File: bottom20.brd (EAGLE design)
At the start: 160 x 100 mm, 141 parts

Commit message: - bot.sch (corrections)
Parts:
- removed 5V-SCHALTREGLER1:C3: 100uF, 16V, ±20 %, iceberg20:CAPACITOR-THT-6.3
- removed 5V-SCHALTREGLER1:C4: 1000uF, 25V, ±20 %, iceberg20:CAPACITOR-THT-10
- removed 5V-SCHALTREGLER1:D1: 1N5822, iceberg20:DO-201AD
- removed 5V-SCHALTREGLER1:IC2: LM2576, iceberg20:TO220-5PIN
- removed 5V-SCHALTREGLER1:L1: L-100U, iceberg20:PISR
- removed 5V-SCHALTREGLER1:R1: 100k, iceberg20:R0805
- removed ARDUINO1:R4: 1k, iceberg20:R0805
- added ANSCHLUSS1:J1: 5V-ARD, iceberg20:JUMPER-SJ-3
- added PHOTOTRANSISTOR1:R17, PHOTOTRANSISTOR2:R17: 330, iceberg20:R0805
- added SCHALTREGLER1:X3: SCHALTREGLER, iceberg20:5X1
- ANSCHLUSS1:X1: value FTDI-Adapter -> FTDI
- ANSCHLUSS1:X2: value CON-UP -> WANNENSTECKER-14; device iceberg20:PIN-HEADER-ANGLED-6 -> iceberg20:2X7
- ARDUINO1:R3: value R -> 330
- moved ARDUINO1:C7 1574.2 mm to (-12.4, 20.6)
- moved ARDUINO1:IC1 1574.2 mm to (-22.6, 24.4)
- moved PHOTOTRANSISTOR2:T9 1515.7 mm to (-7.25, 0.00)
- moved PHOTOTRANSISTOR2:T8 1491.3 mm to (0.00, -58.0), turned to 90 degrees
- moved PHOTOTRANSISTOR2:T7 1488.4 mm to (0.00, -51.2), turned to 90 degrees
- moved PHOTOTRANSISTOR2:T6 1485.7 mm to (0.00, -44.0), turned to 90 degrees
- moved PHOTOTRANSISTOR2:T5 1483.4 mm to (0.00, -36.2), turned to 90 degrees
- moved PHOTOTRANSISTOR2:T4 1480.8 mm to (0.00, -29.0), turned to 90 degrees
- moved PHOTOTRANSISTOR2:T3 1478.1 mm to (0.00, -22.2), turned to 90 degrees
- moved PHOTOTRANSISTOR2:T2 1475.7 mm to (0.00, -15.0), turned to 90 degrees
- moved PHOTOTRANSISTOR2:T1 1434.2 mm to (0.00, -7.25), turned to 90 degrees
- moved PHOTOTRANSISTOR2:T10 1430.0 mm to (-15.0, 0.00)
- moved PHOTOTRANSISTOR2:T11 1429.2 mm to (-22.2, 0.00)
- moved PHOTOTRANSISTOR2:T12 1428.8 mm to (-29.0, 0.00)
- moved PHOTOTRANSISTOR2:T13 1428.0 mm to (-36.2, 0.00)
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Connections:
- net ARDUINO1:D10 renamed ARDUINO1:SS
- removed net 5V-SCHALTREGLER1:N$1: 5V-SCHALTREGLER1:IC2.5, 5V-SCHALTREGLER1:R1.1
- removed net 5V-SCHALTREGLER1:N$2: 5V-SCHALTREGLER1:D1.1, 5V-SCHALTREGLER1:IC2.2, 5V-SCHALTREGLER1:L1.1
- removed net ANSCHLUSS1:N$1: ANSCHLUSS1:X2.P$5
- removed net ARD-IN: ANSCHLUSS1:X2.P$1, ARDUINO1:IC1.10
- removed net ARD-RST: ANSCHLUSS1:X1.P$6, ARDUINO1:C1.1
- removed net ARDUINO1:N$1: ARDUINO1:C1.2, ARDUINO1:IC1.29, ARDUINO1:R3.1, ARDUINO1:S1.A1, ARDUINO1:S1.A2
- removed net BIT0: PHOTOTRANSISTOR2:IC1.11
- removed net BIT1: PHOTOTRANSISTOR2:IC1.10
- removed net BIT2: PHOTOTRANSISTOR2:IC1.14
- removed net BIT3: PHOTOTRANSISTOR2:IC1.13
- removed net BITA0: ARDUINO1:IC1.23
- removed net BITA1: ARDUINO1:IC1.24
- removed net BITA2: ARDUINO1:IC1.25
- removed net BITA3: ARDUINO1:IC1.26
- removed net BITB0: ARDUINO1:IC1.2
- removed net BITB1: ARDUINO1:IC1.9
- removed net BITB2: ARDUINO1:IC1.12
- removed net BITB3: ARDUINO1:IC1.13
- removed net PHOTOTRANSISTOR1:BIT0: PHOTOTRANSISTOR1:IC1.11
- removed net PHOTOTRANSISTOR1:BIT1: PHOTOTRANSISTOR1:IC1.10
- removed net PHOTOTRANSISTOR1:BIT2: PHOTOTRANSISTOR1:IC1.14
- removed net PHOTOTRANSISTOR1:BIT3: PHOTOTRANSISTOR1:IC1.13
- removed net PHOTOTRANSISTOR2:BIT0: PHOTOTRANSISTOR2:IC1.11
- removed net PHOTOTRANSISTOR2:BIT1: PHOTOTRANSISTOR2:IC1.10
- removed net PHOTOTRANSISTOR2:BIT2: PHOTOTRANSISTOR2:IC1.14
- removed net PHOTOTRANSISTOR2:BIT3: PHOTOTRANSISTOR2:IC1.13
- new net 5V-ARD: ANSCHLUSS1:J1.2, ARDUINO1:C2.1, ARDUINO1:C3.1, ARDUINO1:C4.1, ARDUINO1:IC1.18, ARDUINO1:IC1.4, ARDUINO1:IC1.6, ARDUINO1:R3.2
- new net ANSCHLUSS1:CTS: ANSCHLUSS1:X1.2
- new net ANSCHLUSS1:VID: ANSCHLUSS1:J1.1, ANSCHLUSS1:X1.3
- new net ARD-INTERUPT: ANSCHLUSS1:X2.2
- new net ARD-RESET: ANSCHLUSS1:X2.13, ARDUINO1:C1.2, ARDUINO1:IC1.29, ARDUINO1:R3.1, ARDUINO1:S1.A1, ARDUINO1:S1.A2
- new net ARDUINO1:ARD-IN: ARDUINO1:IC1.10
- new net DTR: ANSCHLUSS1:X1.6, ARDUINO1:C1.1
- new net N$11: ARDUINO1:IC1.26, PHOTOTRANSISTOR1:IC1.11
- new net N$12: ARDUINO1:IC1.19, PHOTOTRANSISTOR1:IC1.15, PHOTOTRANSISTOR1:R17.2
- new net N$3: ARDUINO1:IC1.1, PHOTOTRANSISTOR2:IC1.15, PHOTOTRANSISTOR2:R17.2
- new net N$7: ARDUINO1:IC1.13, PHOTOTRANSISTOR2:IC1.13
- new net N$8: ARDUINO1:IC1.23, PHOTOTRANSISTOR1:IC1.13
- new net N$9: ARDUINO1:IC1.24, PHOTOTRANSISTOR1:IC1.14
- net +12V: now also SCHALTREGLER1:X3.3; no longer 5V-SCHALTREGLER1:C3.1, 5V-SCHALTREGLER1:IC2.1
- net +5V: now also ANSCHLUSS1:J1.3, PHOTOTRANSISTOR1:R17.1, PHOTOTRANSISTOR2:R17.1, SCHALTREGLER1:X3.1; no longer 5V-SCHALTREGLER1:C4.1, 5V-SCHALTREGLER1:IC2.4, 5V-SCHALTREGLER1:L1.2, 5V-SCHALTREGLER1:R1.2, ANSCHLUSS1:X1.P$3
- net GND: now also ANSCHLUSS1:X1.1, ANSCHLUSS1:X2.1, ANSCHLUSS1:X2.14, ANSCHLUSS1:X2.4, ANSCHLUSS1:X2.6, ANSCHLUSS1:X2.8, ANSCHLUSS1:X2.9, SCHALTREGLER1:X3.2; no longer 5V-SCHALTREGLER1:C3.2, 5V-SCHALTREGLER1:C4.2, 5V-SCHALTREGLER1:D1.2, 5V-SCHALTREGLER1:IC2.3, ANSCHLUSS1:X1.P$1, ARDUINO1:R4.1, ARDUINO1:R4.2
- net LED-IN: now also ANSCHLUSS1:X2.5; no longer ANSCHLUSS1:X2.P$4
- net N$1: now also ANSCHLUSS1:X2.11, ANSCHLUSS1:X2.12, ANSCHLUSS1:X2.3; no longer ANSCHLUSS1:X2.P$6
- net N$10: now also ARDUINO1:IC1.25, PHOTOTRANSISTOR1:IC1.10; no longer ANSCHLUSS1:X1.P$2
- net N$4: now also ARDUINO1:IC1.2, PHOTOTRANSISTOR2:IC1.11; no longer ARDUINO1:IC1.1, PHOTOTRANSISTOR2:IC1.15
- net N$5: now also ARDUINO1:IC1.9, PHOTOTRANSISTOR2:IC1.10; no longer ARDUINO1:C2.1, ARDUINO1:C3.1, ARDUINO1:C4.1, ARDUINO1:IC1.18, ARDUINO1:IC1.4, ARDUINO1:IC1.6, ARDUINO1:R3.2
- net N$6: now also ARDUINO1:IC1.12, PHOTOTRANSISTOR2:IC1.14; no longer ARDUINO1:IC1.19, PHOTOTRANSISTOR1:IC1.15
- net RX: now also ANSCHLUSS1:X1.5, ARDUINO1:R1.2; no longer ANSCHLUSS1:X1.P$5, ARDUINO1:R2.2
- net SCL: now also ANSCHLUSS1:X2.10; no longer ANSCHLUSS1:X2.P$3
- net SDA: now also ANSCHLUSS1:X2.7; no longer ANSCHLUSS1:X2.P$2
- net TX: now also ANSCHLUSS1:X1.4, ARDUINO1:R2.2; no longer ANSCHLUSS1:X1.P$4, ARDUINO1:R1.2
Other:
- board size 160 x 100 mm -> 160 x 140 mm

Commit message: - bot.brd (layout)
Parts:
- removed ANSCHLUSS1:J1: 5V-ARD, iceberg20:JUMPER-SJ-3
- removed ANSCHLUSS1:X1: FTDI, iceberg20:PIN-HEADER-ANGLED-6
- removed ANSCHLUSS1:X2: WANNENSTECKER-14, iceberg20:2X7
- removed ARDUINO1:C1, ARDUINO1:C5, LED1:C1, LED1:C10, LED1:C11, LED1:C12, LED1:C13, LED1:C14, LED1:C15, LED1:C16, LED1:C17, LED1:C2, LED1:C3, LED1:C4, LED1:C5, LED1:C6, LED1:C7, LED1:C8, LED1:C9: 100n, iceberg20:C0805
- removed ARDUINO1:C2, ARDUINO1:C4: 1u, iceberg20:C0805
- removed ARDUINO1:C3: 4,7u, 16V, iceberg20:CAPACITOR-THT-3
- removed ARDUINO1:C6, ARDUINO1:C7: 15p, iceberg20:C0805
- removed ARDUINO1:IC1: ATMEGA328P-AU, iceberg20:ATMEGA328P-AU
- removed ARDUINO1:Q1: 16MHz, iceberg20:CRYSTAL_HC49U-V
- removed ARDUINO1:R1, ARDUINO1:R2: 1k, iceberg20:R0805
- removed ARDUINO1:R3, PHOTOTRANSISTOR1:R17, PHOTOTRANSISTOR2:R17: 330, iceberg20:R0805
- removed ARDUINO1:S1: SMD-BUTTON, iceberg20:SWITCH-6MM-SMD
- removed ARDUINO1:TP1: SCK, iceberg20:TESTPAD_B2,54
- removed ARDUINO1:TP2: MISO, iceberg20:TESTPAD_B2,54
- removed ARDUINO1:TP3: MOSI, iceberg20:TESTPAD_B2,54
- removed ARDUINO1:TP4: SS, iceberg20:TESTPAD_B2,54
- removed LED1:LED26, LED1:LED27, LED1:LED28, LED1:LED29, LED1:LED32: WS2812B, iceberg20:5050
- removed PHOTOTRANSISTOR1:IC1, PHOTOTRANSISTOR2:IC1: MULTIPLEXER, iceberg20:SO24
- removed PHOTOTRANSISTOR1:R1, PHOTOTRANSISTOR1:R10, PHOTOTRANSISTOR1:R11, PHOTOTRANSISTOR1:R12, PHOTOTRANSISTOR1:R13, PHOTOTRANSISTOR1:R14, PHOTOTRANSISTOR1:R15, PHOTOTRANSISTOR1:R16, PHOTOTRANSISTOR1:R2, PHOTOTRANSISTOR1:R3, PHOTOTRANSISTOR1:R4, PHOTOTRANSISTOR1:R5, PHOTOTRANSISTOR1:R6, PHOTOTRANSISTOR1:R7, PHOTOTRANSISTOR1:R8, PHOTOTRANSISTOR1:R9, PHOTOTRANSISTOR2:R1, PHOTOTRANSISTOR2:R10, PHOTOTRANSISTOR2:R11, PHOTOTRANSISTOR2:R12, PHOTOTRANSISTOR2:R13, PHOTOTRANSISTOR2:R14, PHOTOTRANSISTOR2:R15, PHOTOTRANSISTOR2:R16, PHOTOTRANSISTOR2:R2, PHOTOTRANSISTOR2:R3, PHOTOTRANSISTOR2:R4, PHOTOTRANSISTOR2:R5, PHOTOTRANSISTOR2:R6, PHOTOTRANSISTOR2:R7, PHOTOTRANSISTOR2:R8, PHOTOTRANSISTOR2:R9: 20k, iceberg20:R0805
- removed PHOTOTRANSISTOR2:T10, PHOTOTRANSISTOR2:T11, PHOTOTRANSISTOR2:T12, PHOTOTRANSISTOR2:T13, PHOTOTRANSISTOR2:T16: SFH320, iceberg20:PLCC-2
- removed SCHALTREGLER1:X3: SCHALTREGLER, iceberg20:5X1
- added A:C1, A:C5, L:C1, L:C10, L:C11, L:C12, L:C13, L:C14, L:C15, L:C16, L:C17, L:C2, L:C3, L:C4, L:C5, L:C6, L:C7, L:C8, L:C9: 100n, iceberg20:C0805
- added A:C2, A:C4: 1u, iceberg20:C0805
- added A:C3: 4,7u, 16V, iceberg20:CAPACITOR-THT-3
- added A:C6, A:C7: 15p, iceberg20:C0805
- added A:IC1: ATMEGA328P-AU, iceberg20:ATMEGA328P-AU
- added A:Q1: 16MHz, iceberg20:CRYSTAL_HC49U-V
- added A:R3, T1:R17, T2:R17: 330, iceberg20:R0805
- added A:S1: SMD-BUTTON, iceberg20:SWITCH-6MM-SMD
- added A:TP1: SCK, iceberg20:TESTPAD_B2,54
- added A:TP2: MISO, iceberg20:TESTPAD_B2,54
- added A:TP3: MOSI, iceberg20:TESTPAD_B2,54
- added A:TP4: SS, iceberg20:TESTPAD_B2,54
- added L:LED26, L:LED27, L:LED30, L:LED31, L:LED32: WS2812B, iceberg20:5050
- added P:X3: SCHALTREGLER, iceberg20:5X1
- added T1:IC1, T2:IC1: MULTIPLEXER, iceberg20:SO24
- added T1:R1, T1:R10, T1:R11, T1:R12, T1:R13, T1:R14, T1:R15, T1:R16, T1:R2, T1:R3, T1:R4, T1:R5, T1:R6, T1:R7, T1:R8, T1:R9, T2:R1, T2:R10, T2:R11, T2:R12, T2:R13, T2:R14, T2:R15, T2:R16, T2:R2, T2:R3, T2:R4, T2:R5, T2:R6, T2:R7, T2:R8, T2:R9: 20k, iceberg20:R0805
- added T2:T10, T2:T11, T2:T14, T2:T15, T2:T16: SFH320, iceberg20:PLCC-2
- added X:D1: DIODE, iceberg20:DO-214BA
- added X:X1: FTDI, iceberg20:PIN-HEADER-ANGLED-6
- added X:X2: WANNENSTECKER-14, iceberg20:2X7
- renumbered LED1:LED1 to L:LED1, LED1:LED10 to L:LED10, LED1:LED11 to L:LED11, LED1:LED12 to L:LED12, LED1:LED13 to L:LED13, LED1:LED14 to L:LED14, LED1:LED15 to L:LED15, LED1:LED16 to L:LED16, LED1:LED17 to L:LED17, LED1:LED18 to L:LED18, LED1:LED19 to L:LED19, LED1:LED2 to L:LED2, LED1:LED20 to L:LED20, LED1:LED21 to L:LED21, LED1:LED22 to L:LED22, LED1:LED23 to L:LED23, LED1:LED24 to L:LED24, LED1:LED25 to L:LED25, LED1:LED3 to L:LED3, LED1:LED30 to L:LED28, LED1:LED31 to L:LED29, LED1:LED4 to L:LED4, LED1:LED5 to L:LED5, LED1:LED6 to L:LED6, LED1:LED7 to L:LED7, LED1:LED8 to L:LED8, LED1:LED9 to L:LED9, PHOTOTRANSISTOR1:T1 to T1:T1, PHOTOTRANSISTOR1:T10 to T1:T10, PHOTOTRANSISTOR1:T11 to T1:T11, PHOTOTRANSISTOR1:T12 to T1:T12, PHOTOTRANSISTOR1:T13 to T1:T13, PHOTOTRANSISTOR1:T14 to T1:T14, PHOTOTRANSISTOR1:T15 to T1:T15, PHOTOTRANSISTOR1:T16 to T1:T16, PHOTOTRANSISTOR1:T2 to T1:T2, PHOTOTRANSISTOR1:T3 to T1:T3, PHOTOTRANSISTOR1:T4 to T1:T4, PHOTOTRANSISTOR1:T5 to T1:T5, PHOTOTRANSISTOR1:T6 to T1:T6, PHOTOTRANSISTOR1:T7 to T1:T7, PHOTOTRANSISTOR1:T8 to T1:T8, PHOTOTRANSISTOR1:T9 to T1:T9, PHOTOTRANSISTOR2:T1 to T2:T1, PHOTOTRANSISTOR2:T14 to T2:T12, PHOTOTRANSISTOR2:T15 to T2:T13, PHOTOTRANSISTOR2:T2 to T2:T2, PHOTOTRANSISTOR2:T3 to T2:T3, PHOTOTRANSISTOR2:T4 to T2:T4, PHOTOTRANSISTOR2:T5 to T2:T5, PHOTOTRANSISTOR2:T6 to T2:T6, PHOTOTRANSISTOR2:T7 to T2:T7, PHOTOTRANSISTOR2:T8 to T2:T8, PHOTOTRANSISTOR2:T9 to T2:T9
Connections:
- net LED1:CON-1 renamed L:CON-1
- net LED1:CON-2 renamed L:CON-2
- net LED1:CON-3 renamed L:CON-3
- net LED1:LED-IN1 renamed L:LED-IN1
- net LED1:LED-IN10 renamed L:LED-IN10
- net LED1:LED-IN11 renamed L:LED-IN11
- net LED1:LED-IN12 renamed L:LED-IN8
- net LED1:LED-IN2 renamed L:LED-IN2
- net LED1:LED-IN3 renamed L:LED-IN3
- net LED1:LED-IN5 renamed L:LED-IN5
- net LED1:LED-IN6 renamed L:LED-IN6
- net LED1:LED-IN7 renamed L:LED-IN7
- net LED1:LED-IN9 renamed L:LED-IN9
- net LED1:N$1 renamed L:N$1
- net LED1:N$11 renamed L:N$11
- net LED1:N$12 renamed L:N$12
- net LED1:N$13 renamed L:N$13
- net LED1:N$14 renamed L:N$14
- net LED1:N$16 renamed L:N$16
- net LED1:N$17 renamed L:N$17
- net LED1:N$18 renamed L:N$18
- net LED1:N$2 renamed L:N$2
- net LED1:N$4 renamed L:N$4
- net LED1:N$7 renamed L:N$7
- net LED1:N$9 renamed L:N$9
- removed net ANSCHLUSS1:CTS: ANSCHLUSS1:X1.2
- removed net ANSCHLUSS1:VID: ANSCHLUSS1:J1.1, ANSCHLUSS1:X1.3
- removed net ARDUINO1:AIN1: ARDUINO1:IC1.11
- removed net ARDUINO1:ARD-IN: ARDUINO1:IC1.10
- removed net ARDUINO1:N$12: ARDUINO1:IC1.30, ARDUINO1:R1.1
- removed net ARDUINO1:N$13: ARDUINO1:IC1.31, ARDUINO1:R2.1
- removed net ARDUINO1:N$2: ARDUINO1:C7.1, ARDUINO1:IC1.8, ARDUINO1:Q1.1
- removed net ARDUINO1:N$3: ARDUINO1:C6.2, ARDUINO1:IC1.7, ARDUINO1:Q1.2
- removed net ARDUINO1:N$5: ARDUINO1:IC1.15, ARDUINO1:TP3.TP
- removed net ARDUINO1:N$6: ARDUINO1:IC1.16, ARDUINO1:TP2.TP
- removed net ARDUINO1:N$7: ARDUINO1:IC1.17, ARDUINO1:TP1.TP
- removed net ARDUINO1:N$8: ARDUINO1:C5.1, ARDUINO1:IC1.20
- removed net ARDUINO1:SS: ARDUINO1:IC1.14, ARDUINO1:TP4.TP
- removed net LED1:LED-IN4: LED1:LED26.OUT, LED1:LED27.IN
- removed net LED1:LED-IN8: LED1:LED28.OUT, LED1:LED29.IN
- removed net LED1:N$3: L:LED25.OUT, LED1:LED26.IN
- removed net LED1:N$5: LED1:LED27.OUT, LED1:LED28.IN
- removed net LED1:N$6: L:LED28.IN, LED1:LED29.OUT
- removed net LED1:N$8: L:LED29.OUT, LED1:LED32.IN
- removed net PHOTOTRANSISTOR1:N$1: PHOTOTRANSISTOR1:IC1.9, PHOTOTRANSISTOR1:R1.1, T1:T1.A
- removed net PHOTOTRANSISTOR1:N$10: PHOTOTRANSISTOR1:IC1.3, PHOTOTRANSISTOR1:R7.1, T1:T7.A
- removed net PHOTOTRANSISTOR1:N$11: PHOTOTRANSISTOR1:IC1.4, PHOTOTRANSISTOR1:R6.1, T1:T6.A
- removed net PHOTOTRANSISTOR1:N$12: PHOTOTRANSISTOR1:IC1.17, PHOTOTRANSISTOR1:R10.1, T1:T10.A
- removed net PHOTOTRANSISTOR1:N$14: PHOTOTRANSISTOR1:IC1.18, PHOTOTRANSISTOR1:R11.1, T1:T11.A
- removed net PHOTOTRANSISTOR1:N$18: PHOTOTRANSISTOR1:IC1.20, PHOTOTRANSISTOR1:R13.1, T1:T13.A
- removed net PHOTOTRANSISTOR1:N$2: PHOTOTRANSISTOR1:IC1.8, PHOTOTRANSISTOR1:R2.1, T1:T2.A
- removed net PHOTOTRANSISTOR1:N$20: PHOTOTRANSISTOR1:IC1.21, PHOTOTRANSISTOR1:R14.1, T1:T14.A
- removed net PHOTOTRANSISTOR1:N$22: PHOTOTRANSISTOR1:IC1.22, PHOTOTRANSISTOR1:R15.1, T1:T15.A
- removed net PHOTOTRANSISTOR1:N$25: PHOTOTRANSISTOR1:IC1.23, PHOTOTRANSISTOR1:R16.1, T1:T16.A
- removed net PHOTOTRANSISTOR1:N$26: PHOTOTRANSISTOR1:IC1.19, PHOTOTRANSISTOR1:R12.1, T1:T12.A
- removed net PHOTOTRANSISTOR1:N$3: PHOTOTRANSISTOR1:IC1.7, PHOTOTRANSISTOR1:R3.1, T1:T3.A
- removed net PHOTOTRANSISTOR1:N$4: PHOTOTRANSISTOR1:IC1.6, PHOTOTRANSISTOR1:R4.1, T1:T4.A
- removed net PHOTOTRANSISTOR1:N$5: PHOTOTRANSISTOR1:IC1.5, PHOTOTRANSISTOR1:R5.1, T1:T5.A
- removed net PHOTOTRANSISTOR1:N$7: PHOTOTRANSISTOR1:IC1.16, PHOTOTRANSISTOR1:R9.1, T1:T9.A
- removed net PHOTOTRANSISTOR1:N$9: PHOTOTRANSISTOR1:IC1.2, PHOTOTRANSISTOR1:R8.1, T1:T8.A
- removed net PHOTOTRANSISTOR2:N$1: PHOTOTRANSISTOR2:IC1.9, PHOTOTRANSISTOR2:R1.1, T2:T1.A
- removed net PHOTOTRANSISTOR2:N$10: PHOTOTRANSISTOR2:IC1.3, PHOTOTRANSISTOR2:R7.1, T2:T7.A
- removed net PHOTOTRANSISTOR2:N$11: PHOTOTRANSISTOR2:IC1.4, PHOTOTRANSISTOR2:R6.1, T2:T6.A
- removed net PHOTOTRANSISTOR2:N$12: PHOTOTRANSISTOR2:IC1.17, PHOTOTRANSISTOR2:R10.1, PHOTOTRANSISTOR2:T10.A
- removed net PHOTOTRANSISTOR2:N$14: PHOTOTRANSISTOR2:IC1.18, PHOTOTRANSISTOR2:R11.1, PHOTOTRANSISTOR2:T11.A
- removed net PHOTOTRANSISTOR2:N$18: PHOTOTRANSISTOR2:IC1.20, PHOTOTRANSISTOR2:R13.1, PHOTOTRANSISTOR2:T13.A
- removed net PHOTOTRANSISTOR2:N$2: PHOTOTRANSISTOR2:IC1.8, PHOTOTRANSISTOR2:R2.1, T2:T2.A
- removed net PHOTOTRANSISTOR2:N$20: PHOTOTRANSISTOR2:IC1.21, PHOTOTRANSISTOR2:R14.1, T2:T12.A
- removed net PHOTOTRANSISTOR2:N$22: PHOTOTRANSISTOR2:IC1.22, PHOTOTRANSISTOR2:R15.1, T2:T13.A
- removed net PHOTOTRANSISTOR2:N$25: PHOTOTRANSISTOR2:IC1.23, PHOTOTRANSISTOR2:R16.1, PHOTOTRANSISTOR2:T16.A
- removed net PHOTOTRANSISTOR2:N$26: PHOTOTRANSISTOR2:IC1.19, PHOTOTRANSISTOR2:R12.1, PHOTOTRANSISTOR2:T12.A
- removed net PHOTOTRANSISTOR2:N$3: PHOTOTRANSISTOR2:IC1.7, PHOTOTRANSISTOR2:R3.1, T2:T3.A
- removed net PHOTOTRANSISTOR2:N$4: PHOTOTRANSISTOR2:IC1.6, PHOTOTRANSISTOR2:R4.1, T2:T4.A
- removed net PHOTOTRANSISTOR2:N$5: PHOTOTRANSISTOR2:IC1.5, PHOTOTRANSISTOR2:R5.1, T2:T5.A
- removed net PHOTOTRANSISTOR2:N$7: PHOTOTRANSISTOR2:IC1.16, PHOTOTRANSISTOR2:R9.1, T2:T9.A
- removed net PHOTOTRANSISTOR2:N$9: PHOTOTRANSISTOR2:IC1.2, PHOTOTRANSISTOR2:R8.1, T2:T8.A
- new net A:AIN1: A:IC1.11
- new net A:ARD-IN: A:IC1.10
- new net A:N$2: A:C7.1, A:IC1.8, A:Q1.1
- new net A:N$3: A:C6.2, A:IC1.7, A:Q1.2
- new net A:N$5: A:IC1.15, A:TP3.TP
- new net A:N$6: A:IC1.16, A:TP2.TP
- new net A:N$7: A:IC1.17, A:TP1.TP
- new net A:N$8: A:C5.1, A:IC1.20
- new net A:SS: A:IC1.14, A:TP4.TP
- new net L:LED-IN12: L:LED30.OUT, L:LED31.IN
- new net L:LED-IN4: L:LED26.OUT, L:LED27.IN
- new net L:N$3: L:LED25.OUT, L:LED26.IN
- new net L:N$5: L:LED27.OUT, L:LED28.IN
- new net L:N$6: L:LED29.OUT, L:LED30.IN
- new net L:N$8: L:LED31.OUT, L:LED32.IN
- new net T1:N$1: T1:IC1.9, T1:R1.1, T1:T1.A
- new net T1:N$10: T1:IC1.3, T1:R7.1, T1:T7.A
- new net T1:N$11: T1:IC1.4, T1:R6.1, T1:T6.A
- new net T1:N$12: T1:IC1.17, T1:R10.1, T1:T10.A
- new net T1:N$14: T1:IC1.18, T1:R11.1, T1:T11.A
- new net T1:N$18: T1:IC1.20, T1:R13.1, T1:T13.A
- new net T1:N$2: T1:IC1.8, T1:R2.1, T1:T2.A
- new net T1:N$20: T1:IC1.21, T1:R14.1, T1:T14.A
- new net T1:N$22: T1:IC1.22, T1:R15.1, T1:T15.A
- new net T1:N$25: T1:IC1.23, T1:R16.1, T1:T16.A
- new net T1:N$26: T1:IC1.19, T1:R12.1, T1:T12.A
- new net T1:N$3: T1:IC1.7, T1:R3.1, T1:T3.A
- new net T1:N$4: T1:IC1.6, T1:R4.1, T1:T4.A
- new net T1:N$5: T1:IC1.5, T1:R5.1, T1:T5.A
- new net T1:N$7: T1:IC1.16, T1:R9.1, T1:T9.A
- new net T1:N$9: T1:IC1.2, T1:R8.1, T1:T8.A
- new net T2:N$1: T2:IC1.9, T2:R1.1, T2:T1.A
- new net T2:N$10: T2:IC1.3, T2:R7.1, T2:T7.A
- new net T2:N$11: T2:IC1.4, T2:R6.1, T2:T6.A
- new net T2:N$12: T2:IC1.17, T2:R10.1, T2:T10.A
- new net T2:N$14: T2:IC1.18, T2:R11.1, T2:T11.A
- new net T2:N$18: T2:IC1.20, T2:R13.1, T2:T13.A
- new net T2:N$2: T2:IC1.8, T2:R2.1, T2:T2.A
- new net T2:N$20: T2:IC1.21, T2:R14.1, T2:T14.A
- new net T2:N$22: T2:IC1.22, T2:R15.1, T2:T15.A
- new net T2:N$25: T2:IC1.23, T2:R16.1, T2:T16.A
- new net T2:N$26: T2:IC1.19, T2:R12.1, T2:T12.A
- new net T2:N$3: T2:IC1.7, T2:R3.1, T2:T3.A
- new net T2:N$4: T2:IC1.6, T2:R4.1, T2:T4.A
- new net T2:N$5: T2:IC1.5, T2:R5.1, T2:T5.A
- new net T2:N$7: T2:IC1.16, T2:R9.1, T2:T9.A
- new net T2:N$9: T2:IC1.2, T2:R8.1, T2:T8.A
- new net X:CTS: X:X1.2
- new net X:VID: X:D1.2, X:X1.3
- net +12V: now also P:X3.3; no longer SCHALTREGLER1:X3.3
- net +5V: now also L:C1.1, L:C10.1, L:C11.1, L:C12.1, L:C13.1, L:C14.1, L:C15.1, L:C16.1, L:C17.1, L:C2.1, L:C3.1, L:C4.1, L:C5.1, L:C6.1, L:C7.1, L:C8.1, L:C9.1, L:LED26.VDD, L:LED27.VDD, L:LED30.VDD, L:LED31.VDD, L:LED32.VDD, P:X3.1, T1:IC1.24, T1:R1.2, T1:R10.2, T1:R11.2, T1:R12.2, T1:R13.2, T1:R14.2, T1:R15.2, T1:R16.2, T1:R17.1, T1:R2.2, T1:R3.2, T1:R4.2, T1:R5.2, T1:R6.2, T1:R7.2, T1:R8.2, T1:R9.2, T2:IC1.24, T2:R1.2, T2:R10.2, T2:R11.2, T2:R12.2, T2:R13.2, T2:R14.2, T2:R15.2, T2:R16.2, T2:R17.1, T2:R2.2, T2:R3.2, T2:R4.2, T2:R5.2, T2:R6.2, T2:R7.2, T2:R8.2, T2:R9.2, X:D1.1; no longer ANSCHLUSS1:J1.3, LED1:C1.1, LED1:C10.1, LED1:C11.1, LED1:C12.1, LED1:C13.1, LED1:C14.1, LED1:C15.1, LED1:C16.1, LED1:C17.1, LED1:C2.1, LED1:C3.1, LED1:C4.1, LED1:C5.1, LED1:C6.1, LED1:C7.1, LED1:C8.1, LED1:C9.1, LED1:LED26.VDD, LED1:LED27.VDD, LED1:LED28.VDD, LED1:LED29.VDD, LED1:LED32.VDD, PHOTOTRANSISTOR1:IC1.24, PHOTOTRANSISTOR1:R1.2, PHOTOTRANSISTOR1:R10.2, PHOTOTRANSISTOR1:R11.2, PHOTOTRANSISTOR1:R12.2, PHOTOTRANSISTOR1:R13.2, PHOTOTRANSISTOR1:R14.2, PHOTOTRANSISTOR1:R15.2, PHOTOTRANSISTOR1:R16.2, PHOTOTRANSISTOR1:R17.1, PHOTOTRANSISTOR1:R2.2, PHOTOTRANSISTOR1:R3.2, PHOTOTRANSISTOR1:R4.2, PHOTOTRANSISTOR1:R5.2, PHOTOTRANSISTOR1:R6.2, PHOTOTRANSISTOR1:R7.2, PHOTOTRANSISTOR1:R8.2, PHOTOTRANSISTOR1:R9.2, PHOTOTRANSISTOR2:IC1.24, PHOTOTRANSISTOR2:R1.2, PHOTOTRANSISTOR2:R10.2, PHOTOTRANSISTOR2:R11.2, PHOTOTRANSISTOR2:R12.2, PHOTOTRANSISTOR2:R13.2, PHOTOTRANSISTOR2:R14.2, PHOTOTRANSISTOR2:R15.2, PHOTOTRANSISTOR2:R16.2, PHOTOTRANSISTOR2:R17.1, PHOTOTRANSISTOR2:R2.2, PHOTOTRANSISTOR2:R3.2, PHOTOTRANSISTOR2:R4.2, PHOTOTRANSISTOR2:R5.2, PHOTOTRANSISTOR2:R6.2, PHOTOTRANSISTOR2:R7.2, PHOTOTRANSISTOR2:R8.2, PHOTOTRANSISTOR2:R9.2, SCHALTREGLER1:X3.1
- net 5V-ARD: now also A:C2.1, A:C3.1, A:C4.1, A:IC1.18, A:IC1.4, A:IC1.6, A:R3.2; no longer ANSCHLUSS1:J1.2, ARDUINO1:C2.1, ARDUINO1:C3.1, ARDUINO1:C4.1, ARDUINO1:IC1.18, ARDUINO1:IC1.4, ARDUINO1:IC1.6, ARDUINO1:R3.2
- net ARD-INTERUPT: now also X:X2.2; no longer ANSCHLUSS1:X2.2
- net ARD-RESET: now also A:C1.2, A:IC1.29, A:R3.1, A:S1.A1, A:S1.A2, X:X2.13; no longer ANSCHLUSS1:X2.13, ARDUINO1:C1.2, ARDUINO1:IC1.29, ARDUINO1:R3.1, ARDUINO1:S1.A1, ARDUINO1:S1.A2
- net DTR: now also A:C1.1, X:X1.6; no longer ANSCHLUSS1:X1.6, ARDUINO1:C1.1
- net GND: now also A:C2.2, A:C3.2, A:C4.2, A:C5.2, A:C6.1, A:C7.2, A:IC1.21, A:IC1.3, A:IC1.5, A:S1.B1, A:S1.B2, L:C1.2, L:C10.2, L:C11.2, L:C12.2, L:C13.2, L:C14.2, L:C15.2, L:C16.2, L:C17.2, L:C2.2, L:C3.2, L:C4.2, L:C5.2, L:C6.2, L:C7.2, L:C8.2, L:C9.2, L:LED26.GND, L:LED27.GND, L:LED30.GND, L:LED31.GND, L:LED32.GND, P:X3.2, T1:IC1.12, T2:IC1.12, T2:T10.C, T2:T11.C, T2:T14.C, T2:T15.C, T2:T16.C, X:X1.1, X:X2.1, X:X2.14, X:X2.4, X:X2.6, X:X2.8, X:X2.9; no longer ANSCHLUSS1:X1.1, ANSCHLUSS1:X2.1, ANSCHLUSS1:X2.14, ANSCHLUSS1:X2.4, ANSCHLUSS1:X2.6, ANSCHLUSS1:X2.8, ANSCHLUSS1:X2.9, ARDUINO1:C2.2, ARDUINO1:C3.2, ARDUINO1:C4.2, ARDUINO1:C5.2, ARDUINO1:C6.1, ARDUINO1:C7.2, ARDUINO1:IC1.21, ARDUINO1:IC1.3, ARDUINO1:IC1.5, ARDUINO1:S1.B1, ARDUINO1:S1.B2, LED1:C1.2, LED1:C10.2, LED1:C11.2, LED1:C12.2, LED1:C13.2, LED1:C14.2, LED1:C15.2, LED1:C16.2, LED1:C17.2, LED1:C2.2, LED1:C3.2, LED1:C4.2, LED1:C5.2, LED1:C6.2, LED1:C7.2, LED1:C8.2, LED1:C9.2, LED1:LED26.GND, LED1:LED27.GND, LED1:LED28.GND, LED1:LED29.GND, LED1:LED32.GND, PHOTOTRANSISTOR1:IC1.12, PHOTOTRANSISTOR2:IC1.12, PHOTOTRANSISTOR2:T10.C, PHOTOTRANSISTOR2:T11.C, PHOTOTRANSISTOR2:T12.C, PHOTOTRANSISTOR2:T13.C, PHOTOTRANSISTOR2:T16.C, SCHALTREGLER1:X3.2
- net LED-IN: now also X:X2.5; no longer ANSCHLUSS1:X2.5
- net N$1: now also X:X2.11, X:X2.12, X:X2.3; no longer ANSCHLUSS1:X2.11, ANSCHLUSS1:X2.12, ANSCHLUSS1:X2.3
- net N$10: now also A:IC1.25, T1:IC1.10; no longer ARDUINO1:IC1.25, PHOTOTRANSISTOR1:IC1.10
- net N$11: now also A:IC1.26, T1:IC1.11; no longer ARDUINO1:IC1.26, PHOTOTRANSISTOR1:IC1.11
- net N$12: now also A:IC1.19, T1:IC1.15, T1:R17.2; no longer ARDUINO1:IC1.19, PHOTOTRANSISTOR1:IC1.15, PHOTOTRANSISTOR1:R17.2
- net N$13: now also A:IC1.22, T1:IC1.1; no longer ARDUINO1:IC1.22, PHOTOTRANSISTOR1:IC1.1
- net N$2: now also A:IC1.32, T2:IC1.1; no longer ARDUINO1:IC1.32, PHOTOTRANSISTOR2:IC1.1
- net N$3: now also A:IC1.1, T2:IC1.15, T2:R17.2; no longer ARDUINO1:IC1.1, PHOTOTRANSISTOR2:IC1.15, PHOTOTRANSISTOR2:R17.2
- net N$4: now also A:IC1.2, T2:IC1.11; no longer ARDUINO1:IC1.2, PHOTOTRANSISTOR2:IC1.11
- net N$5: now also A:IC1.9, T2:IC1.10; no longer ARDUINO1:IC1.9, PHOTOTRANSISTOR2:IC1.10
- net N$6: now also A:IC1.12, T2:IC1.14; no longer ARDUINO1:IC1.12, PHOTOTRANSISTOR2:IC1.14
- net N$7: now also A:IC1.13, T2:IC1.13; no longer ARDUINO1:IC1.13, PHOTOTRANSISTOR2:IC1.13
- net N$8: now also A:IC1.23, T1:IC1.13; no longer ARDUINO1:IC1.23, PHOTOTRANSISTOR1:IC1.13
- net N$9: now also A:IC1.24, T1:IC1.14; no longer ARDUINO1:IC1.24, PHOTOTRANSISTOR1:IC1.14
- net RX: now also A:IC1.30, X:X1.5; no longer ANSCHLUSS1:X1.5, ARDUINO1:R1.2
- net SCL: now also A:IC1.28, X:X2.10; no longer ANSCHLUSS1:X2.10, ARDUINO1:IC1.28
- net SDA: now also A:IC1.27, X:X2.7; no longer ANSCHLUSS1:X2.7, ARDUINO1:IC1.27
- net TX: now also A:IC1.31, X:X1.4; no longer ANSCHLUSS1:X1.4, ARDUINO1:R2.2
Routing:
- added copper zone on layer 16, net GND

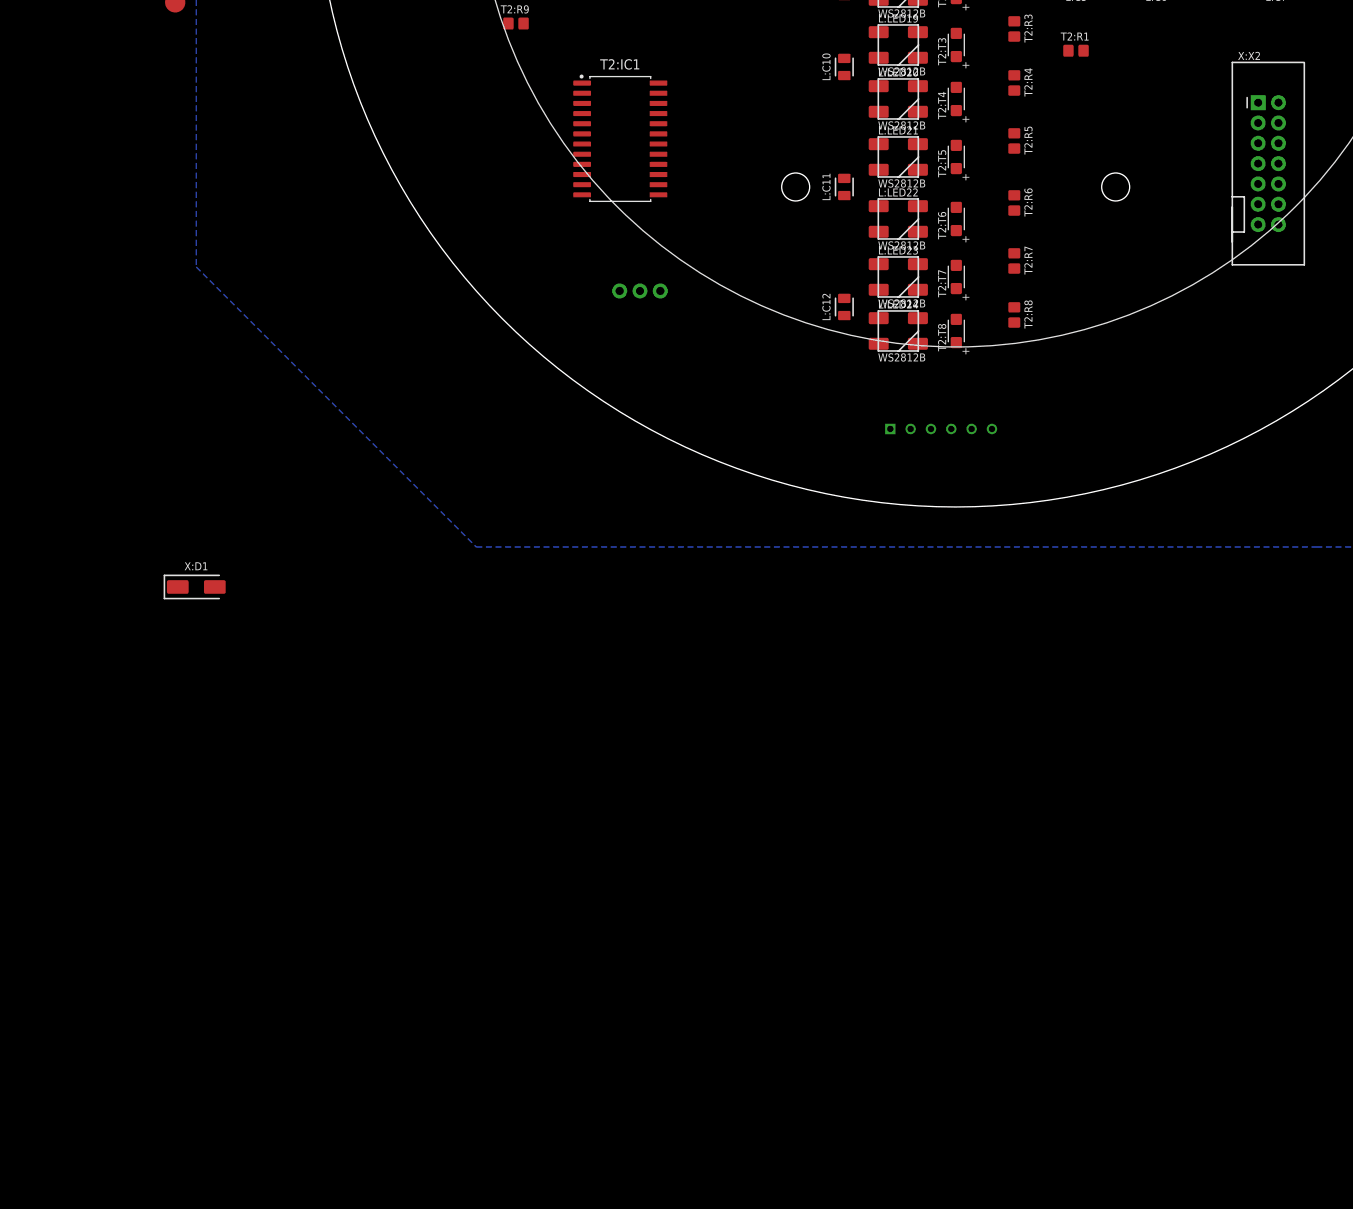
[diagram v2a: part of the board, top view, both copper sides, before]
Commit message: - bot.sch (corrections)
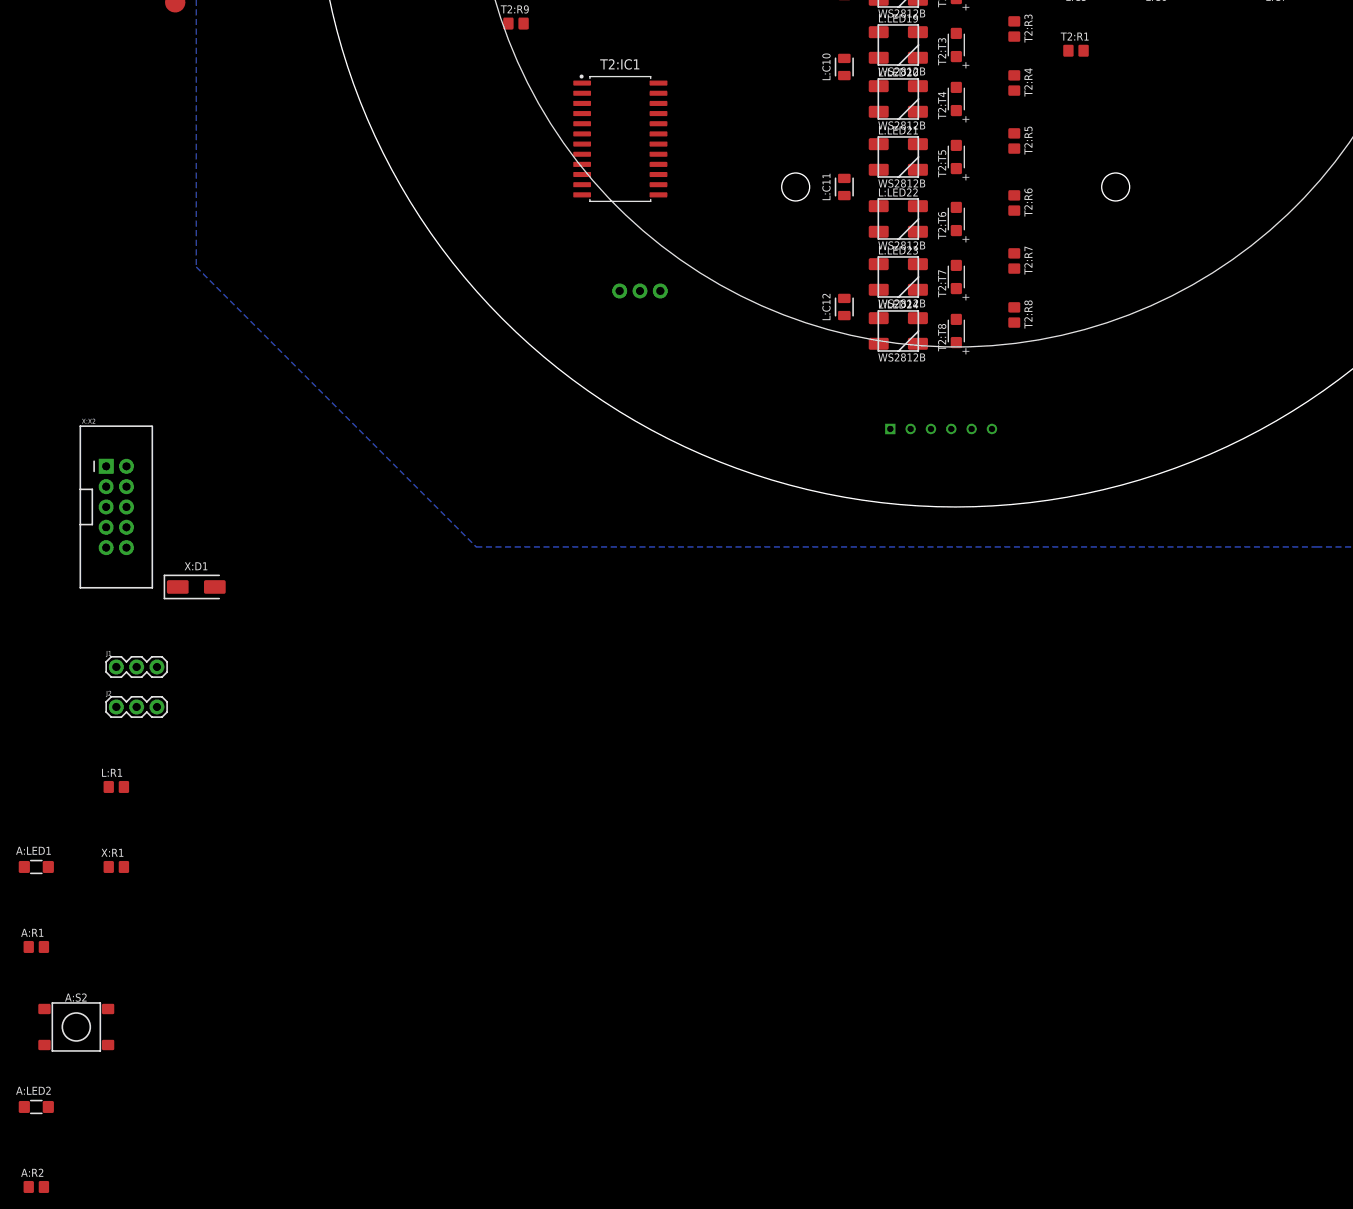
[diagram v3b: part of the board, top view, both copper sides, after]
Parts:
- added A:LED1, A:LED2: LED-GREEN1, iceberg20:1206
- added A:R1, A:R2: 110, iceberg20:R0805
- added A:S2: SMD-BUTTON, iceberg20:SWITCH-6MM-SMD
- added J1: TX, iceberg20:3X1
- added J2: RX, iceberg20:3X1
- added L:R1, X:R1: 330, iceberg20:R0805
- A:R3: value 330 -> 100k
- L:C1: value 100n -> 1u
- T1:R17, T2:R17: value 330 -> 10k
- X:X2: value WANNENSTECKER-14 -> WANNENSTECKER-10; device iceberg20:2X7 -> iceberg20:2X5-SHROUDED
- moved X:X2 151.8 mm to (-105.0, -80.0)
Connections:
- net A:ARD-IN renamed ARD-INTERRUPT
- removed net 5V-ARD: A:C2.1, A:C3.1, A:C4.1, A:IC1.18, A:IC1.4, A:IC1.6, A:R3.2
- removed net A:AIN1: A:IC1.11
- removed net ARD-INTERUPT: X:X2.2
- removed net SCL: A:IC1.28, X:X2.10
- removed net SDA: A:IC1.27, X:X2.7
- new net A:N$1: A:IC1.11, A:R1.1
- new net A:N$10: A:LED2.A, A:R2.2
- new net A:N$11: A:IC1.28, A:R2.1
- new net A:N$4: A:LED1.A, A:R1.2
- new net A:N$9: A:IC1.27, A:S2.A1, A:S2.A2
- new net ARD-RX: J2.3
- new net ARD-TX: J1.3
- new net L:N$10: L:LED1.IN, L:R1.1
- new net N$14: A:IC1.31, J1.2
- new net N$15: A:IC1.30, J2.2
- new net X:ARD-INTERRUPT: X:R1.2
- new net X:ARD-RX: X:X2.3
- new net X:ARD-TX: X:X2.4
- new net X:LED-IN: X:X2.6
- new net X:N$1: X:R1.1, X:X2.8
- net +5V: now also A:C2.1, A:C3.1, A:C4.1, A:IC1.18, A:IC1.4, A:IC1.6, A:R3.2
- net ARD-RESET: now also X:X2.10; no longer X:X2.13
- net GND: now also A:LED1.C, A:LED2.C, A:S2.B1, A:S2.B2, X:X2.7; no longer X:X2.14, X:X2.4, X:X2.6, X:X2.8
- net LED-IN: now also L:R1.2; no longer L:LED1.IN, X:X2.5
- net N$1: now also X:X2.2, X:X2.5; no longer X:X2.11, X:X2.12, X:X2.3
- net RX: now also J2.1; no longer A:IC1.30
- net TX: now also J1.1; no longer A:IC1.31
